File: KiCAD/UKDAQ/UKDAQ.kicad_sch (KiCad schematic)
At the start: 23 parts

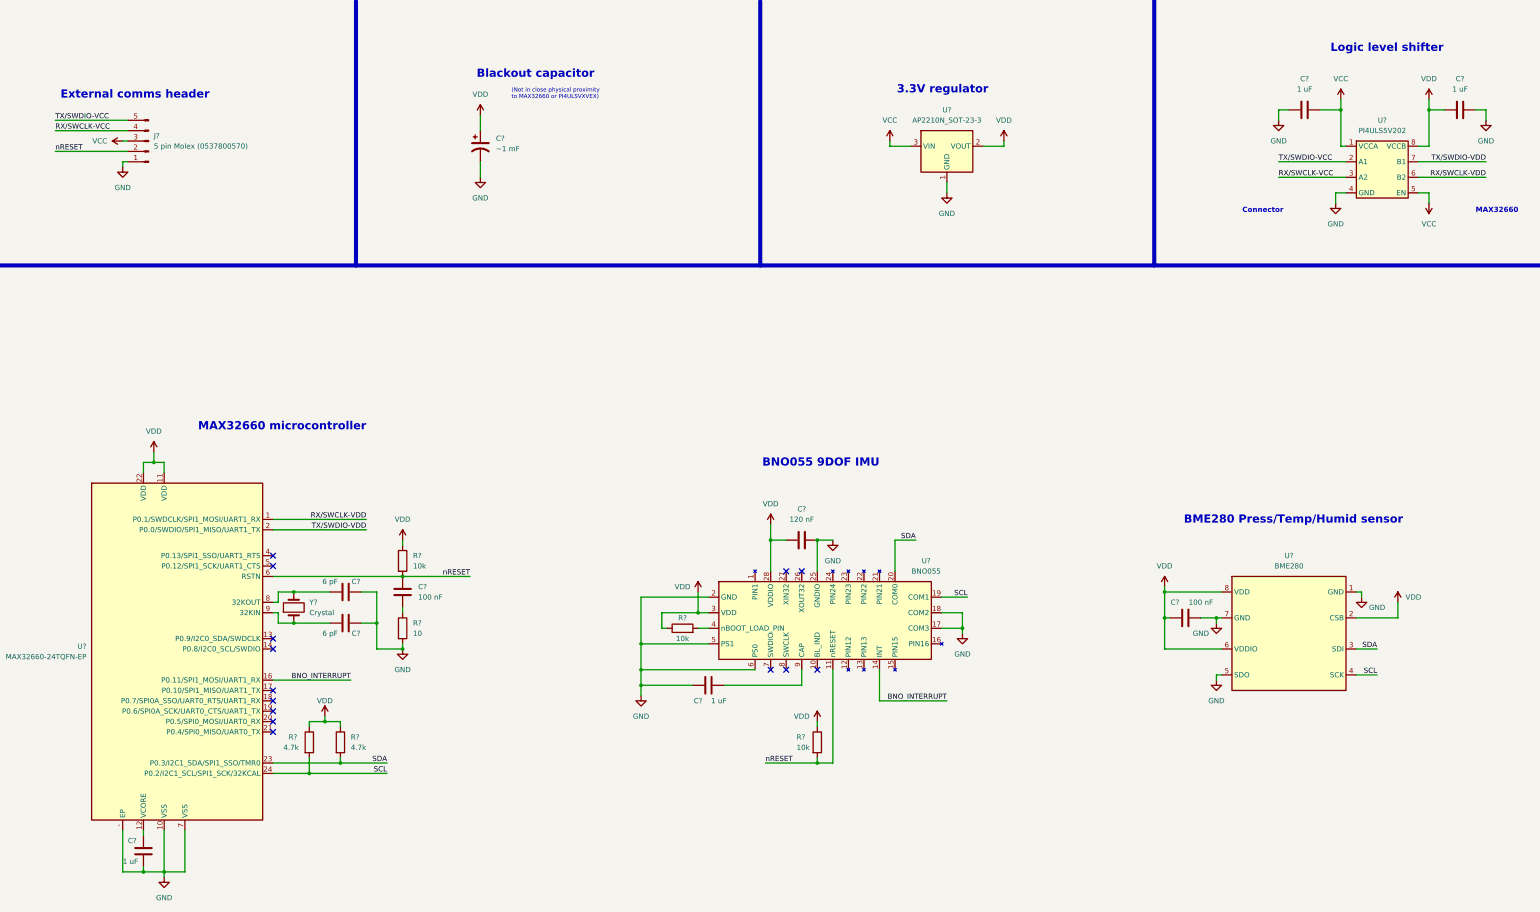
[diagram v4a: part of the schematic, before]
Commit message: made some corrections via the design rule checker. Some complaints about power pins but itll probably be fine.
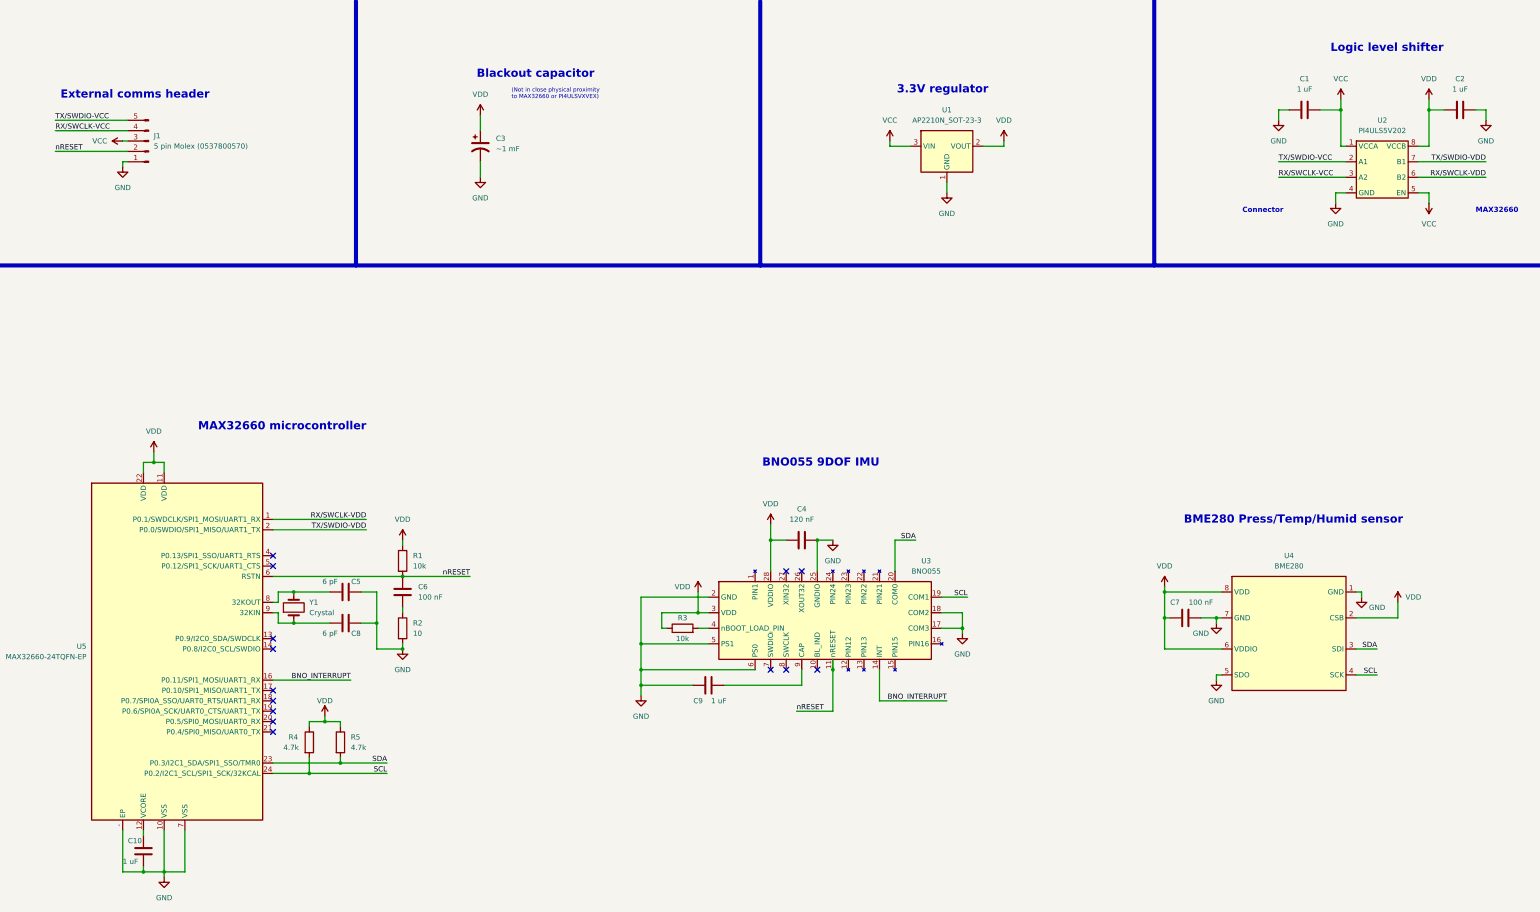
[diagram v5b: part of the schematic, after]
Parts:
- removed R?: 10k, symbol Device:R
- gave numbers to parts that had none: 22

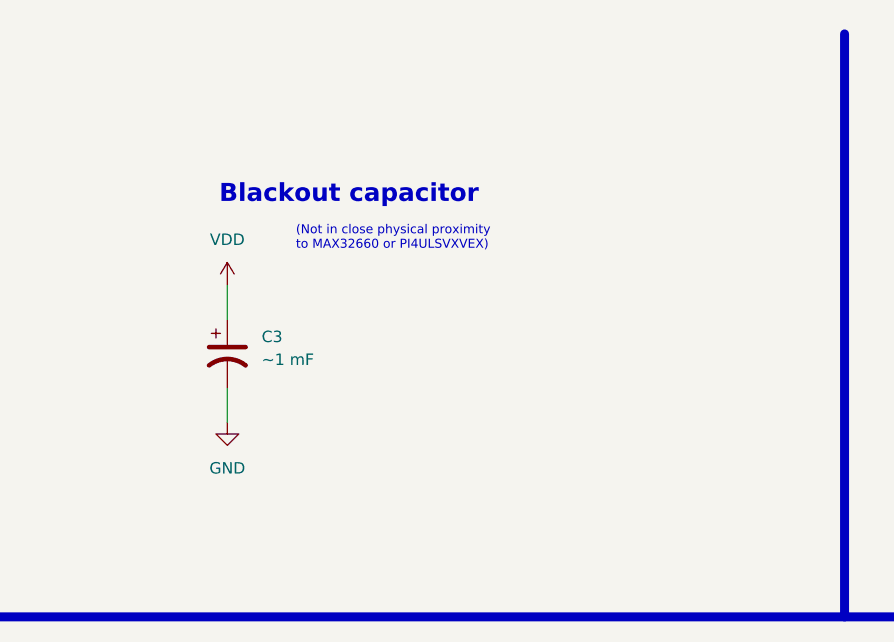
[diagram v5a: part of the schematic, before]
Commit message: untangled the rats nest in PCB editor
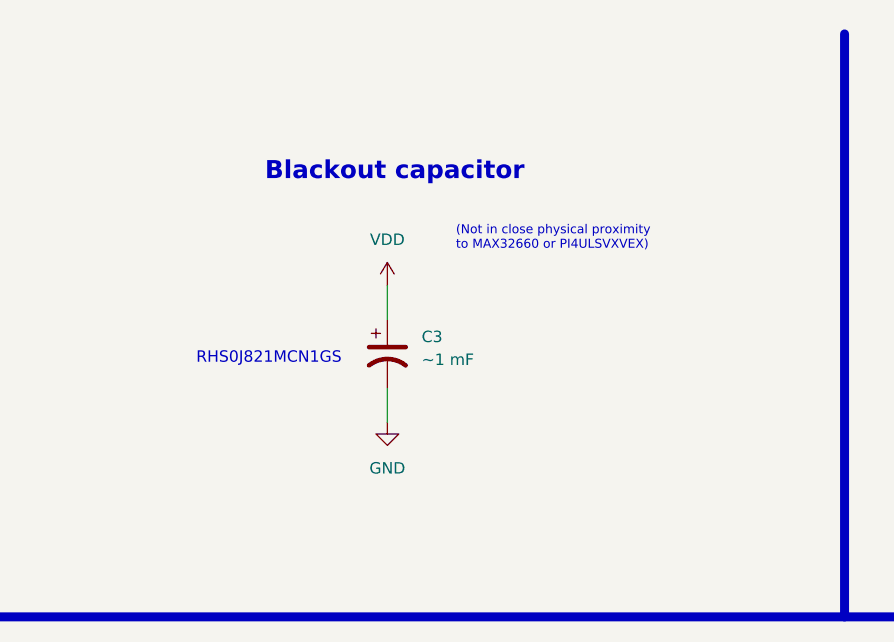
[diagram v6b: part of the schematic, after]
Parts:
- C1, C10, C2, C9: footprint (none) -> Capacitor_SMD:C_0201_0603Metric
- C3: footprint (none) -> Joseph:Can Capacitor - 493-3773-1-ND
- C4, C6, C7: footprint (none) -> Capacitor_SMD:C_0603_1608Metric
- C5, C8: footprint (none) -> Capacitor_SMD:C_01005_0402Metric
- J1: footprint (none) -> Connector_PinHeader_2.54mm:PinHeader_1x05_P2.54mm_Vertical
- R1, R3, R4, R5: footprint (none) -> Resistor_SMD:R_0402_1005Metric
- R2: footprint (none) -> Resistor_SMD:R_0201_0603Metric
- U1: footprint (none) -> Package_TO_SOT_SMD:SOT-23
- U2: footprint (none) -> Package_DFN_QFN:OnSemi_UDFN-8_1.2x1.8mm_P0.4mm
- U3: footprint (none) -> Joseph:LGA28R50P4X10_380X520X100
- U4: footprint (none) -> Joseph:BME280
- U5: footprint (none) -> Joseph:MAX32660-24-TQFN-EP
- Y1: footprint (none) -> Crystal:Crystal_SMD_3215-2Pin_3.2x1.5mm
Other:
- note added: "RHS0J821MCN1GS"
- moved on the sheet: C3
